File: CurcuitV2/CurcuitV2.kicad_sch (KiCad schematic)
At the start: 90 parts, among them IC1 AS5600-ASOT, J1 Conn_01x07, J2 Conn_01x03, J3 Conn_01x02, J4 Conn_01x02, Q1 Q_NMOS_DGS, Q2 Q_NMOS_DGS, Q3 Q_NMOS_DGS, Q4 Q_NMOS_DGS, Q5 Q_NMOS_DGS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

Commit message: ちょっとした修正
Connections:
- net +3V3: now also R24.2
- net at J1.2 (Pin_2), U4.1 (VIN): no longer R24.2
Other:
- moved on the sheet: D13, R24
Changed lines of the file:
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@@
 	)
 	(junction
-		(at 123.19 78.74)
-		(diameter 0)
-		(color 0 0 0 0)
-	)
-	(junction
 		(at 29.21 109.22)
 		(diameter 0)
@@
 	(wire
 		(pts
-			(xy 123.19 91.44) (xy 123.19 86.36)
+			(xy 71.12 143.51) (xy 71.12 140.97)
 		)
 		(stroke
@@
 	(wire
 		(pts
-			(xy 123.19 99.06) (xy 123.19 101.6)
-		)
-		(stroke
-			(width 0)
-			(type default)
-		)
-	)
-	(wire
-		(pts
 			(xy 132.08 175.26) (xy 132.08 177.8)
 		)
@@
 	(wire
 		(pts
-			(xy 118.11 78.74) (xy 123.19 78.74)
+			(xy 118.11 78.74) (xy 130.81 78.74)
 		)
 		(stroke
@@
 	(wire
 		(pts
-			(xy 261.62 29.21) (xy 261.62 26.67)
+			(xy 71.12 130.81) (xy 71.12 133.35)
 		)
 		(stroke
@@
 	(wire
 		(pts
-			(xy 123.19 78.74) (xy 130.81 78.74)
+			(xy 261.62 29.21) (xy 261.62 26.67)
 		)
 		(stroke
@@
 	(wire
 		(pts
+			(xy 71.12 151.13) (xy 71.12 153.67)
+		)
+		(stroke
+			(width 0)
+			(type default)
+		)
+	)
+	(wire
+		(pts
 			(xy 243.84 90.17) (xy 246.38 90.17)
 		)
@@
 	)
 	(symbol
+		(lib_id "power:+3V3")
+		(at 71.12 130.81 0)
+		(unit 1)
+		(exclude_from_sim no)
+		(in_bom yes)
+		(on_board yes)
+		(dnp no)
+		(property "Reference" "#PWR047"
+			(at 71.12 134.62 0)
+			(effects
+				(font
+					(size 1.27 1.27)
+				)
+				(hide yes)
+			)
+		)
+		(property "Value" "+3V3"
+			(at 71.12 127.254 0)
+			(effects
+				(font
+					(size 1.27 1.27)
+				)
+			)
+		)
+		(property "Footprint" ""
+			(at 71.12 130.81 0)
+			(effects
+				(font
+					(size 1.27 1.27)
+				)
+				(hide yes)
+			)
+		)
+		(property "Datasheet" ""
+			(at 71.12 130.81 0)
+			(effects
+				(font
+					(size 1.27 1.27)
+				)
+				(hide yes)
+			)
+		)
+		(property "Description" "Power symbol creates a global label with name \"+3V3\""
+			(at 71.12 130.81 0)
+			(effects
+				(font
+					(size 1.27 1.27)
+				)
+				(hide yes)
+			)
+		)
+		(pin "1"
+		)
+		(instances
+			(project "CurcuitV2"
+				(path "/181931d1-2c3c-43ab-8337-eaba460a1744"
+					(reference "#PWR047")
+					(unit 1)
+				)
+			)
+		)
+	)
+	(symbol
 		(lib_id "power:GND")
 		(at 138.43 88.9 0)
@@
 	(symbol
 		(lib_id "Device:R")
-		(at 123.19 82.55 180)
+		(at 71.12 137.16 180)
 		(unit 1)
 		(exclude_from_sim no)
@@
 		(dnp no)
 		(property "Reference" "R24"
-			(at 123.19 82.55 90)
+			(at 71.12 137.16 90)
 			(effects
 				(font
@@
 		)
 		(property "Value" "1k"
-			(at 121.158 82.55 90)
+			(at 69.088 137.16 90)
 			(effects
 				(font
@@
 		)
 		(property "Footprint" "Resistor_SMD:R_0603_1608Metric"
-			(at 124.968 82.55 90)
+			(at 72.898 137.16 90)
 			(effects
 				(font
@@
 		)
 		(property "Datasheet" "~"
-			(at 123.19 82.55 0)
+			(at 71.12 137.16 0)
 			(effects
 				(font
@@
 		)
 		(property "Description" "Resistor"
-			(at 123.19 82.55 0)
+			(at 71.12 137.16 0)
 			(effects
 				(font
@@
 	(symbol
 		(lib_id "Device:LED")
-		(at 123.19 95.25 90)
+		(at 71.12 147.32 90)
 		(unit 1)
 		(exclude_from_sim no)
@@
 		(dnp no)
 		(property "Reference" "D13"
-			(at 121.158 95.25 0)
+			(at 69.088 147.32 0)
 			(effects
 				(font
@@
 		)
 		(property "Value" "LED"
-			(at 125.476 95.25 0)
+			(at 73.406 147.32 0)
 			(effects
 				(font
@@
 		)
 		(property "Footprint" "LED_SMD:LED_0603_1608Metric"
-			(at 123.19 95.25 0)
+			(at 71.12 147.32 0)
 			(effects
 				(font
@@
 		)
 		(property "Datasheet" "~"
-			(at 123.19 95.25 0)
+			(at 71.12 147.32 0)
 			(effects
 				(font
@@
 		)
 		(property "Description" "Light emitting diode"
-			(at 123.19 95.25 0)
+			(at 71.12 147.32 0)
 			(effects
 				(font
@@
 	(symbol
 		(lib_id "power:GND")
-		(at 123.19 101.6 0)
-		(unit 1)
-		(exclude_from_sim no)
-		(in_bom yes)
-		(on_board yes)
-		(dnp no)
-		(property "Reference" "#PWR047"
-			(at 123.19 107.95 0)
-			(effects
-				(font
-					(size 1.27 1.27)
-				)
-				(hide yes)
-			)
-		)
-		(property "Value" "GND"
-			(at 123.19 105.41 0)
-			(effects
-				(font
-					(size 1.27 1.27)
-				)
-			)
-		)
-		(property "Footprint" ""
-			(at 123.19 101.6 0)
-			(effects
-				(font
-					(size 1.27 1.27)
-				)
-				(hide yes)
-			)
-		)
-		(property "Datasheet" ""
-			(at 123.19 101.6 0)
-			(effects
-				(font
-					(size 1.27 1.27)
-				)
-				(hide yes)
-			)
-		)
-		(property "Description" "Power symbol creates a global label with name \"GND\" , ground"
-			(at 123.19 101.6 0)
-			(effects
-				(font
-					(size 1.27 1.27)
-				)
-				(hide yes)
-			)
-		)
-		(pin "1"
-		)
-		(instances
-			(project "CurcuitV2"
-				(path "/181931d1-2c3c-43ab-8337-eaba460a1744"
-					(reference "#PWR047")
-					(unit 1)
-				)
-			)
-		)
-	)
-	(symbol
-		(lib_id "power:GND")
 		(at 40.64 36.83 0)
 		(unit 1)
@@
 					(unit 1)
 				)
+			)
+		)
+	)
+	(symbol
+		(lib_id "power:GND")
+		(at 71.12 153.67 0)
+		(unit 1)
+		(exclude_from_sim no)
+		(in_bom yes)
+		(on_board yes)
+		(dnp no)
+		(property "Reference" "#PWR048"
+			(at 71.12 160.02 0)
+			(effects
+				(font
+					(size 1.27 1.27)
+				)
+				(hide yes)
+			)
+		)
+		(property "Value" "GND"
+			(at 71.12 157.48 0)
+			(effects
+				(font
+					(size 1.27 1.27)
+				)
+			)
+		)
+		(property "Footprint" ""
+			(at 71.12 153.67 0)
+			(effects
+				(font
+					(size 1.27 1.27)
+				)
+				(hide yes)
+			)
+		)
+		(property "Datasheet" ""
+			(at 71.12 153.67 0)
+			(effects
+				(font
+					(size 1.27 1.27)
+				)
+				(hide yes)
+			)
+		)
+		(property "Description" "Power symbol creates a global label with name \"GND\" , ground"
+			(at 71.12 153.67 0)
+			(effects
+				(font
+					(size 1.27 1.27)
+				)
+				(hide yes)
+			)
+		)
+		(pin "1"
+		)
+		(instances
+			(project "CurcuitV2"
+				(path "/181931d1-2c3c-43ab-8337-eaba460a1744"
+					(reference "#PWR048")
+					(unit 1)
+				)

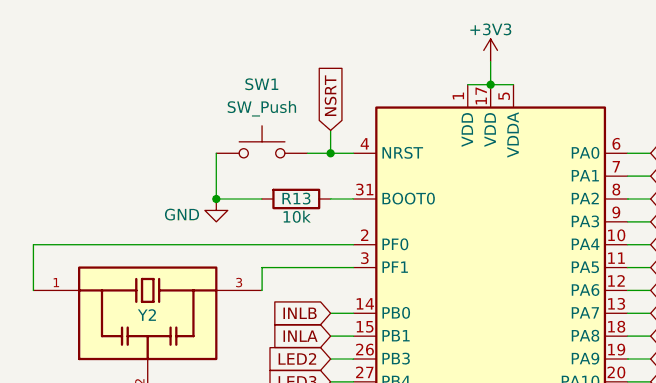
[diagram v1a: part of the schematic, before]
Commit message: NRSTのプルアップ
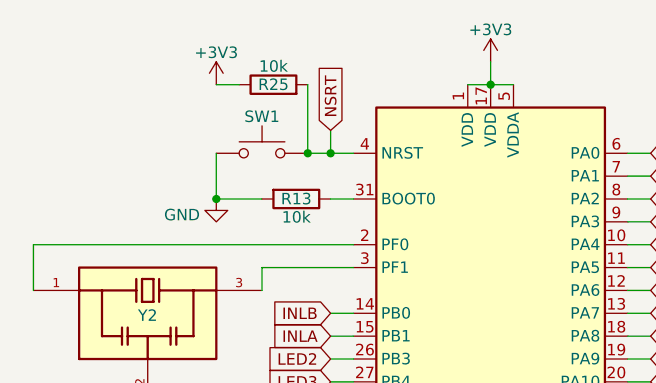
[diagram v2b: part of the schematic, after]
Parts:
- added R25: 10k, Resistor_SMD:R_0603_1608Metric, symbol Device:R
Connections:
- net +3V3: now also R25.1
- net NSRT: now also R25.2
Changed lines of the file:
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@@
 	)
 	(junction
+		(at 50.8 31.75)
+		(diameter 0)
+		(color 0 0 0 0)
+	)
+	(junction
 		(at 57.15 100.33)
 		(diameter 0)
@@
 	(wire
 		(pts
+			(xy 50.8 24.13) (xy 50.8 31.75)
+		)
+		(stroke
+			(width 0)
+			(type default)
+		)
+	)
+	(wire
+		(pts
 			(xy 171.45 36.83) (xy 176.53 36.83)
 		)
@@
 	(wire
 		(pts
+			(xy 40.64 24.13) (xy 43.18 24.13)
+		)
+		(stroke
+			(width 0)
+			(type default)
+		)
+	)
+	(wire
+		(pts
 			(xy 251.46 95.25) (xy 254 95.25)
 		)
@@
 		(on_board yes)
 		(dnp no)
-		(fields_autoplaced yes)
 		(property "Reference" "SW1"
-			(at 45.72 24.13 0)
+			(at 45.72 27.686 0)
 			(effects
 				(font
@@
 					(size 1.27 1.27)
 				)
+				(hide yes)
 			)
 		)
@@
 	)
 	(symbol
+		(lib_id "power:+3V3")
+		(at 40.64 24.13 0)
+		(unit 1)
+		(exclude_from_sim no)
+		(in_bom yes)
+		(on_board yes)
+		(dnp no)
+		(property "Reference" "#PWR049"
+			(at 40.64 27.94 0)
+			(effects
+				(font
+					(size 1.27 1.27)
+				)
+				(hide yes)
+			)
+		)
+		(property "Value" "+3V3"
+			(at 40.64 20.574 0)
+			(effects
+				(font
+					(size 1.27 1.27)
+				)
+			)
+		)
+		(property "Footprint" ""
+			(at 40.64 24.13 0)
+			(effects
+				(font
+					(size 1.27 1.27)
+				)
+				(hide yes)
+			)
+		)
+		(property "Datasheet" ""
+			(at 40.64 24.13 0)
+			(effects
+				(font
+					(size 1.27 1.27)
+				)
+				(hide yes)
+			)
+		)
+		(property "Description" "Power symbol creates a global label with name \"+3V3\""
+			(at 40.64 24.13 0)
+			(effects
+				(font
+					(size 1.27 1.27)
+				)
+				(hide yes)
+			)
+		)
+		(pin "1"
+		)
+		(instances
+			(project "CurcuitV2"
+				(path "/181931d1-2c3c-43ab-8337-eaba460a1744"
+					(reference "#PWR049")
+					(unit 1)
+				)
+			)
+		)
+	)
+	(symbol
 		(lib_id "Mechanical:MountingHole_Pad")
 		(at 33.02 179.07 0)
@@
 					(unit 1)
 				)
+			)
+		)
+	)
+	(symbol
+		(lib_id "Device:R")
+		(at 46.99 24.13 90)
+		(unit 1)
+		(exclude_from_sim no)
+		(in_bom yes)
+		(on_board yes)
+		(dnp no)
+		(property "Reference" "R25"
+			(at 46.99 24.13 90)
+			(effects
+				(font
+					(size 1.27 1.27)
+				)
+			)
+		)
+		(property "Value" "10k"
+			(at 46.99 22.098 90)
+			(effects
+				(font
+					(size 1.27 1.27)
+				)
+			)
+		)
+		(property "Footprint" "Resistor_SMD:R_0603_1608Metric"
+			(at 46.99 25.908 90)
+			(effects
+				(font
+					(size 1.27 1.27)
+				)
+				(hide yes)
+			)
+		)
+		(property "Datasheet" "~"
+			(at 46.99 24.13 0)
+			(effects
+				(font
+					(size 1.27 1.27)
+				)
+				(hide yes)
+			)
+		)
+		(property "Description" "Resistor"
+			(at 46.99 24.13 0)
+			(effects
+				(font
+					(size 1.27 1.27)
+				)
+				(hide yes)
+			)
+		)
+		(pin "1"
+		)
+		(pin "2"
+		)
+		(instances
+			(project "CurcuitV2"
+				(path "/181931d1-2c3c-43ab-8337-eaba460a1744"
+					(reference "R25")
+					(unit 1)
+				)

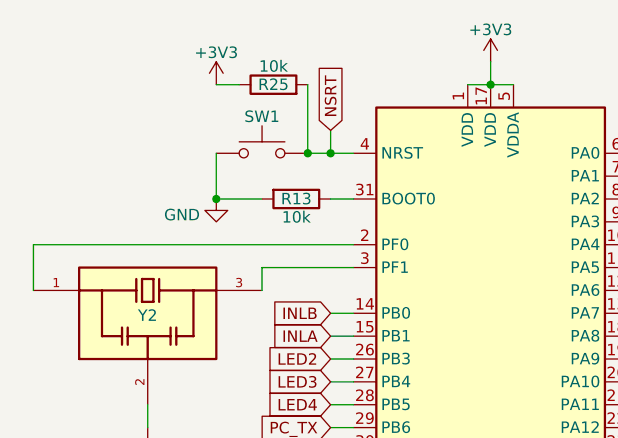
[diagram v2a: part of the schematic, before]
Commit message: NRSTに0.1uf追加
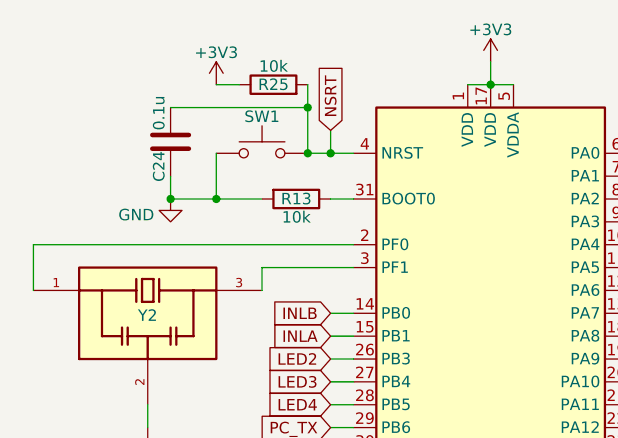
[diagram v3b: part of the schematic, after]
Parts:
- added C24: 0.1u, Capacitor_SMD:C_0603_1608Metric, symbol Device:C
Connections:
- net GND: now also C24.2
- net NSRT: now also C24.1
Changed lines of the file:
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@@
 	)
 	(junction
+		(at 50.8 26.67)
+		(diameter 0)
+		(color 0 0 0 0)
+	)
+	(junction
 		(at 29.21 96.52)
 		(diameter 0)
@@
 	)
 	(junction
+		(at 35.56 36.83)
+		(diameter 0)
+		(color 0 0 0 0)
+	)
+	(junction
 		(at 176.53 24.13)
 		(diameter 0)
@@
 	(wire
 		(pts
-			(xy 50.8 24.13) (xy 50.8 31.75)
+			(xy 50.8 24.13) (xy 50.8 26.67)
 		)
 		(stroke
@@
 	(wire
 		(pts
+			(xy 50.8 26.67) (xy 50.8 31.75)
+		)
+		(stroke
+			(width 0)
+			(type default)
+		)
+	)
+	(wire
+		(pts
 			(xy 127 109.22) (xy 127 111.76)
 		)
@@
 	(wire
 		(pts
+			(xy 35.56 34.29) (xy 35.56 36.83)
+		)
+		(stroke
+			(width 0)
+			(type default)
+		)
+	)
+	(wire
+		(pts
 			(xy 53.34 57.15) (xy 55.88 57.15)
 		)
@@
 	(wire
 		(pts
+			(xy 35.56 26.67) (xy 50.8 26.67)
+		)
+		(stroke
+			(width 0)
+			(type default)
+		)
+	)
+	(wire
+		(pts
 			(xy 69.85 97.79) (xy 69.85 100.33)
 		)
@@
 	(wire
 		(pts
+			(xy 35.56 36.83) (xy 40.64 36.83)
+		)
+		(stroke
+			(width 0)
+			(type default)
+		)
+	)
+	(wire
+		(pts
 			(xy 50.8 31.75) (xy 53.34 31.75)
 		)
@@
 	)
 	(symbol
+		(lib_id "Device:C")
+		(at 35.56 30.48 0)
+		(unit 1)
+		(exclude_from_sim no)
+		(in_bom yes)
+		(on_board yes)
+		(dnp no)
+		(property "Reference" "C24"
+			(at 34.29 31.496 90)
+			(effects
+				(font
+					(size 1.27 1.27)
+				)
+				(justify right)
+			)
+		)
+		(property "Value" "0.1u"
+			(at 34.29 29.21 90)
+			(effects
+				(font
+					(size 1.27 1.27)
+				)
+				(justify left)
+			)
+		)
+		(property "Footprint" "Capacitor_SMD:C_0603_1608Metric"
+			(at 36.5252 34.29 0)
+			(effects
+				(font
+					(size 1.27 1.27)
+				)
+				(hide yes)
+			)
+		)
+		(property "Datasheet" "~"
+			(at 35.56 30.48 0)
+			(effects
+				(font
+					(size 1.27 1.27)
+				)
+				(hide yes)
+			)
+		)
+		(property "Description" "Unpolarized capacitor"
+			(at 35.56 30.48 0)
+			(effects
+				(font
+					(size 1.27 1.27)
+				)
+				(hide yes)
+			)
+		)
+		(pin "1"
+		)
+		(pin "2"
+		)
+		(instances
+			(project "CurcuitV2"
+				(path "/181931d1-2c3c-43ab-8337-eaba460a1744"
+					(reference "C24")
+					(unit 1)
+				)
+			)
+		)
+	)
+	(symbol
 		(lib_id "Switch:SW_Push")
 		(at 45.72 31.75 0)
@@
 	(symbol
 		(lib_id "power:GND")
-		(at 40.64 36.83 0)
+		(at 35.56 36.83 0)
 		(unit 1)
 		(exclude_from_sim no)
@@
 		(dnp no)
 		(property "Reference" "#PWR018"
-			(at 40.64 43.18 0)
+			(at 35.56 43.18 0)
 			(effects
 				(font
@@
 		)
 		(property "Value" "GND"
-			(at 36.83 38.608 0)
+			(at 31.75 38.608 0)
 			(effects
 				(font
@@
 		)
 		(property "Footprint" ""
-			(at 40.64 36.83 0)
+			(at 35.56 36.83 0)
 			(effects
 				(font
@@
 		)
 		(property "Datasheet" ""
-			(at 40.64 36.83 0)
+			(at 35.56 36.83 0)
 			(effects
 				(font
@@
 		)
 		(property "Description" "Power symbol creates a global label with name \"GND\" , ground"
-			(at 40.64 36.83 0)
+			(at 35.56 36.83 0)
 			(effects
 				(font
